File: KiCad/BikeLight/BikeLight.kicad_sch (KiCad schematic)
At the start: 19 parts, among them J1 Conn-01x02_P2.5mm_S2B-XH-A-BK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, J3 Conn-01x02_P2.5mm_S2B-XH-A-BK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, SW1 CK_KMS2xxG, U1 HT-CT62, U2 MPU-6050, U3 MCP1826S-33, U4 MAX17048, U5 TP4056-42-ESOP8, U6 MT3608, U7 RFID-RC522

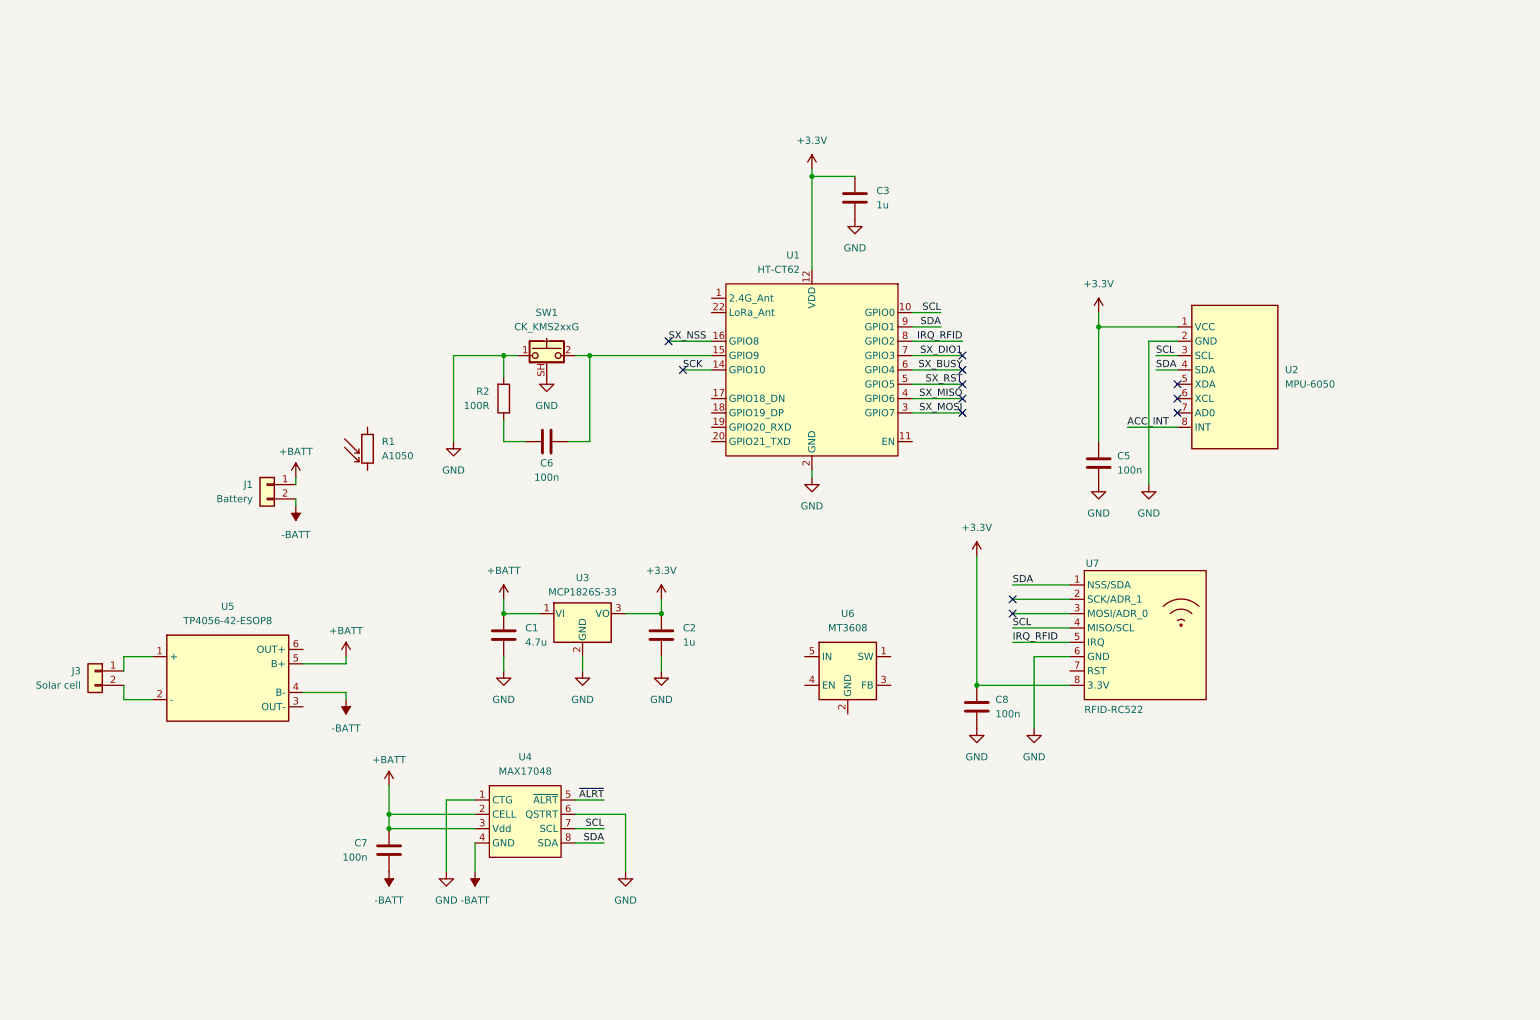
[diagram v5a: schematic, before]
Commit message: Added power protection, annotated
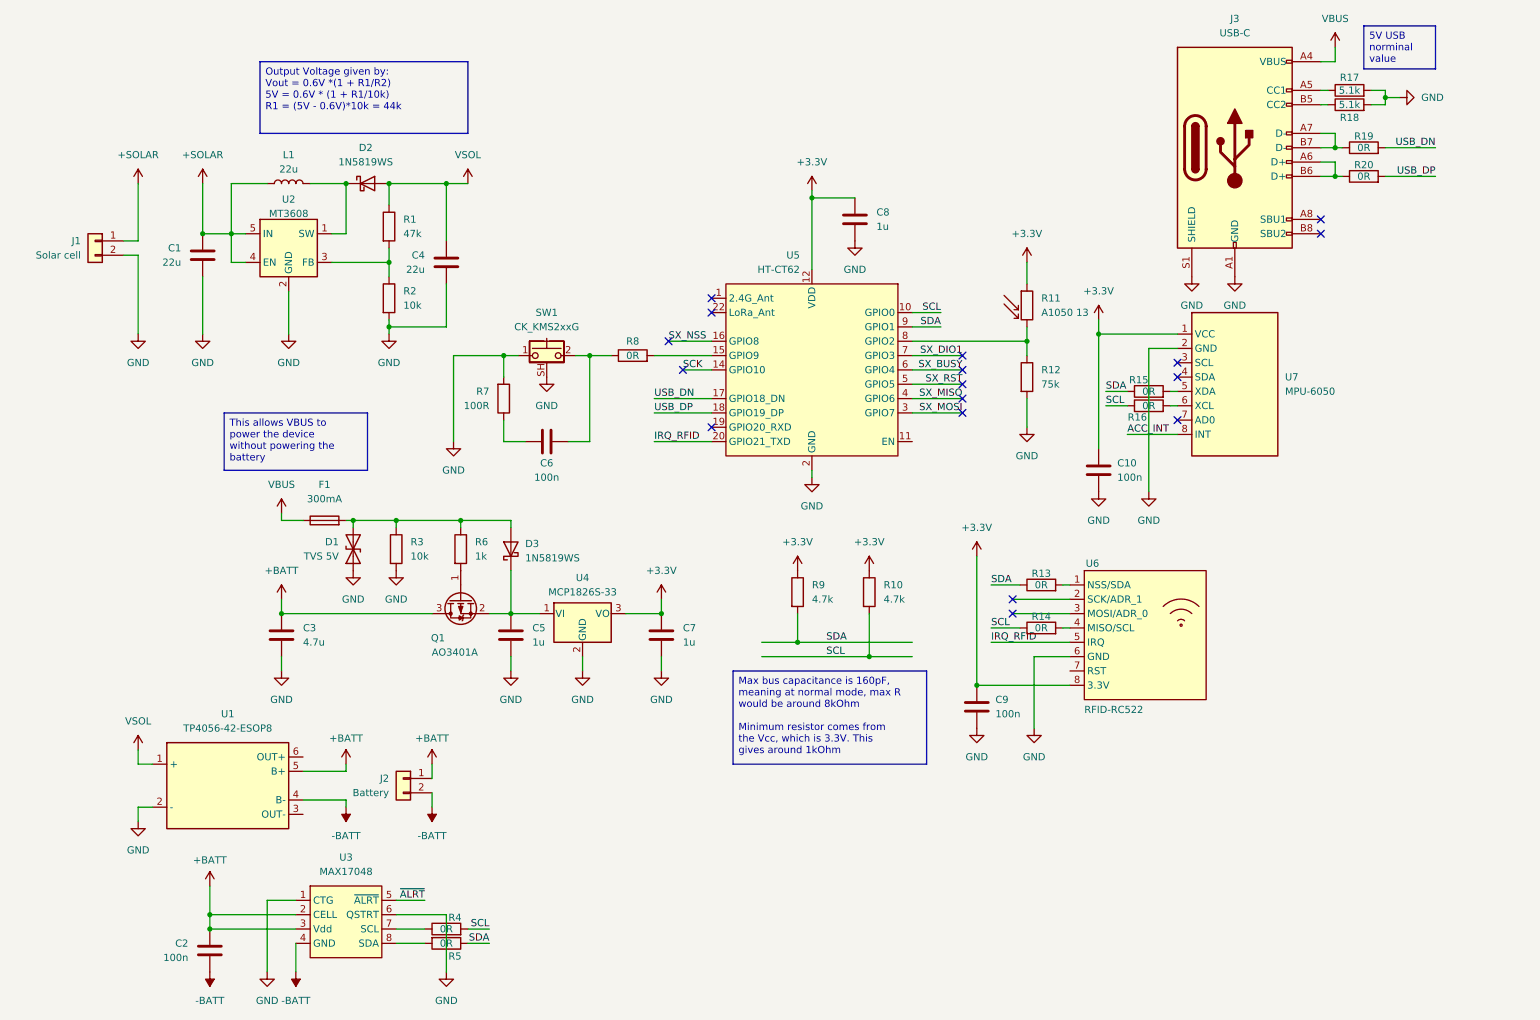
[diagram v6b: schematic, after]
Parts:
- added C1, C4: 22u_0805_CL21A226MAQNNNE, Capacitor_SMD:C_0805_2012Metric, symbol 00-kiml-capacitors-smd:22u_0805_CL21A226MAQNNNE
- added C5: 1u_0603_CL10A105KA8NNNC, Capacitor_SMD:C_0603_1608Metric, symbol 00-kiml-capacitors-smd:1u_0603_CL10A105KA8NNNC
- added D1: SOD-882_0402_RCLAMP0521P-N, Diode_SMD:D_0402_1005Metric, symbol 00-kiml-power-protection:SOD-882_0402_RCLAMP0521P-N
- added D2, D3: 1N5819WS, Diode_SMD:D_SOD-323, symbol 00-kiml-diode:1N5819WS
- added F1: MF-MSMF010-2, Fuse:Fuse_1812_4532Metric, symbol 00-kiml-power-protection:MF-MSMF010-2
- added J3: GT-USB-7051A, Connector_USB:USB_C_Receptacle_G-Switch_GT-USB-7051x, symbol 00-kiml-connector-usb:USB_C_Receptacle_USB2.0_TYPE-C-31-M-12
- added L1: 22u_620mA_1210_CBC3225T220KR, Inductor_SMD:L_1210_3225Metric, symbol 00-kiml-inductors:22u_620mA_1210_CBC3225T220KR
- added Q1: AO3401A, Package_TO_SOT_SMD:SOT-23, symbol 00-kiml-transistor-fet:AO3401A
- added R1: 47k_0402_0402WGF1002TCE, Resistor_SMD:R_0603_1608Metric, symbol 00-kiml-resistors-smd:47k_0402_0402WGF1002TCE
- added R10, R9: 4.7k_0402_0402WGF4701TCE, Resistor_SMD:R_0603_1608Metric, symbol 00-kiml-resistors-smd:4.7k_0402_0402WGF4701TCE
- added R12: 75k_0603_RC0603FR-0775KL, Resistor_SMD:R_0603_1608Metric, symbol 00-kiml-resistors-smd:75k_0603_RC0603FR-0775KL
- added R13, R14, R15, R16, R19, R20, R4, R5, R8: 0R_0603_0603WAF0000T5E, Resistor_SMD:R_0603_1608Metric, symbol 00-kiml-resistors-smd:0R_0603_0603WAF0000T5E
- added R17, R18: 5.1k_0603_0603WAF5101T5E, Resistor_SMD:R_0603_1608Metric, symbol 00-kiml-resistors-smd:5.1k_0603_0603WAF5101T5E
- added R2, R3: 10k_0603_RC0603JR-0710KL, Resistor_SMD:R_0603_1608Metric, symbol 00-kiml-resistors-smd:10k_0603_RC0603JR-0710KL
- added R6: 1k_0603_RMC06031K1%N, Resistor_SMD:R_0603_1608Metric, symbol 00-kiml-resistors-smd:1k_0603_RMC06031K1%N
- R11: renamed from R1; value A1050 -> A1050 13
- renumbered C5 to C10, C7 to C2, C1 to C3, C2 to C7, C3 to C8, C8 to C9, J3 to J1, J1 to J2, R2 to R7, U5 to U1, U6 to U2, U4 to U3, U3 to U4, U1 to U5, U7 to U6, U2 to U7
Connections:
- net +3.3V: now also R11.1, R10.1, R9.1
- net +BATT: now also Q1.3 (D); no longer U4.1 (VI)
- net GND: now also J1.2 (Pin_2), U1.2 (-), U2.2 (GND), C1.2, C4.2, C5.2, D1.1 (A1), J3.A1 (GND), J3.A12 (GND), J3.B1 (GND), J3.B12 (GND), J3.S1 (SHIELD), R12.2, R17.2, R18.2, R2.2, R3.2
- net IRQ_RFID: now also U5.20 (GPIO21_TXD); no longer U5.8 (GPIO2)
- net SCL: now also R10.2, R14.1, R16.1, R4.2; no longer U3.7 (SCL), U6.4 (MISO/SCL), U7.3 (SCL)
- net SDA: now also R13.1, R15.1, R5.1, R9.2; no longer U3.8 (SDA), U6.1 (NSS/SDA), U7.4 (SDA)
- net +SOLAR: now reaches J1.1 (Pin_1)
- net +SOLAR: now also U2.4 (EN), U2.5 (IN), C1.1, L1.1; no longer U1.1 (+)
- net at C6.2, SW1.2: now also R8.1; no longer U5.15 (GPIO9)
- net at U7.5 (XDA): now also R15.2
- net at U7.6 (XCL): now also R16.2
- net USB_DN: now reaches U5.17 (GPIO18_DN)
- net USB_DN: now also R19.2
- net USB_DP: now reaches U5.18 (GPIO19_DP)
- net USB_DP: now also R20.2
- net at U2.1 (SW): now also D2.1 (K), L1.2
- net at U2.3 (FB): now also R1.2, R2.1
- net at R11.2: now also U5.8 (GPIO2), R12.1
- new net: J3.A5 (CC1), R17.1
- new net: J3.A6 (D+), J3.B6 (D+), R20.1
- new net: J3.A7 (D-), J3.B7 (D-), R19.1
- new net: J3.B5 (CC2), R18.1
- new net: D1.2 (A2), D3.2 (A), F1.2, R3.1, R6.1
- new net: R13.2, U6.1 (NSS/SDA)
- new net: R14.2, U6.4 (MISO/SCL)
- new net: C5.1, D3.1 (K), Q1.2 (S), U4.1 (VI)
- new net: R4.1, U3.7 (SCL)
- new net: R5.2, U3.8 (SDA)
- new net: R8.2, U5.15 (GPIO9)
- new net: Q1.1 (G), R6.2
- new net VBUS: F1.1, J3.A4 (VBUS), J3.A9 (VBUS), J3.B4 (VBUS), J3.B9 (VBUS)
- new net VSOL: C4.1, D2.2 (A), R1.1, U1.1 (+)
- no-connect marks 12 -> 17
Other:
- title: (none) -> Bikelight
- moved on the sheet: C10, C2, C3, C8, J1, J2, R11, U1, U2, U3, U7

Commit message: Finished most of the PCB
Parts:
- added R21, R22: 0R_0603_0603WAF0000T5E, Resistor_SMD:R_0603_1608Metric, symbol 00-kiml-resistors-smd:0R_0603_0603WAF0000T5E
- U6: footprint (none) -> Personal_Library:RFID_RC522
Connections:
- net ACC_INT: now also U5.19 (GPIO20_RXD)
- net SCL: now also R22.1
- net SDA: now also R5.2, R21.1; no longer R5.1
- net VSOL: now also D2.1 (K); no longer D2.2 (A)
- net at L1.2, U2.1 (SW): now also D2.2 (A); no longer D2.1 (K)
- net at U7.3 (SCL): now also R22.2
- net at U7.4 (SDA): now also R21.2
- net at U3.8 (SDA): now also R5.1; no longer R5.2
- no-connect marks 17 -> 14
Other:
- moved on the sheet: D2, R5

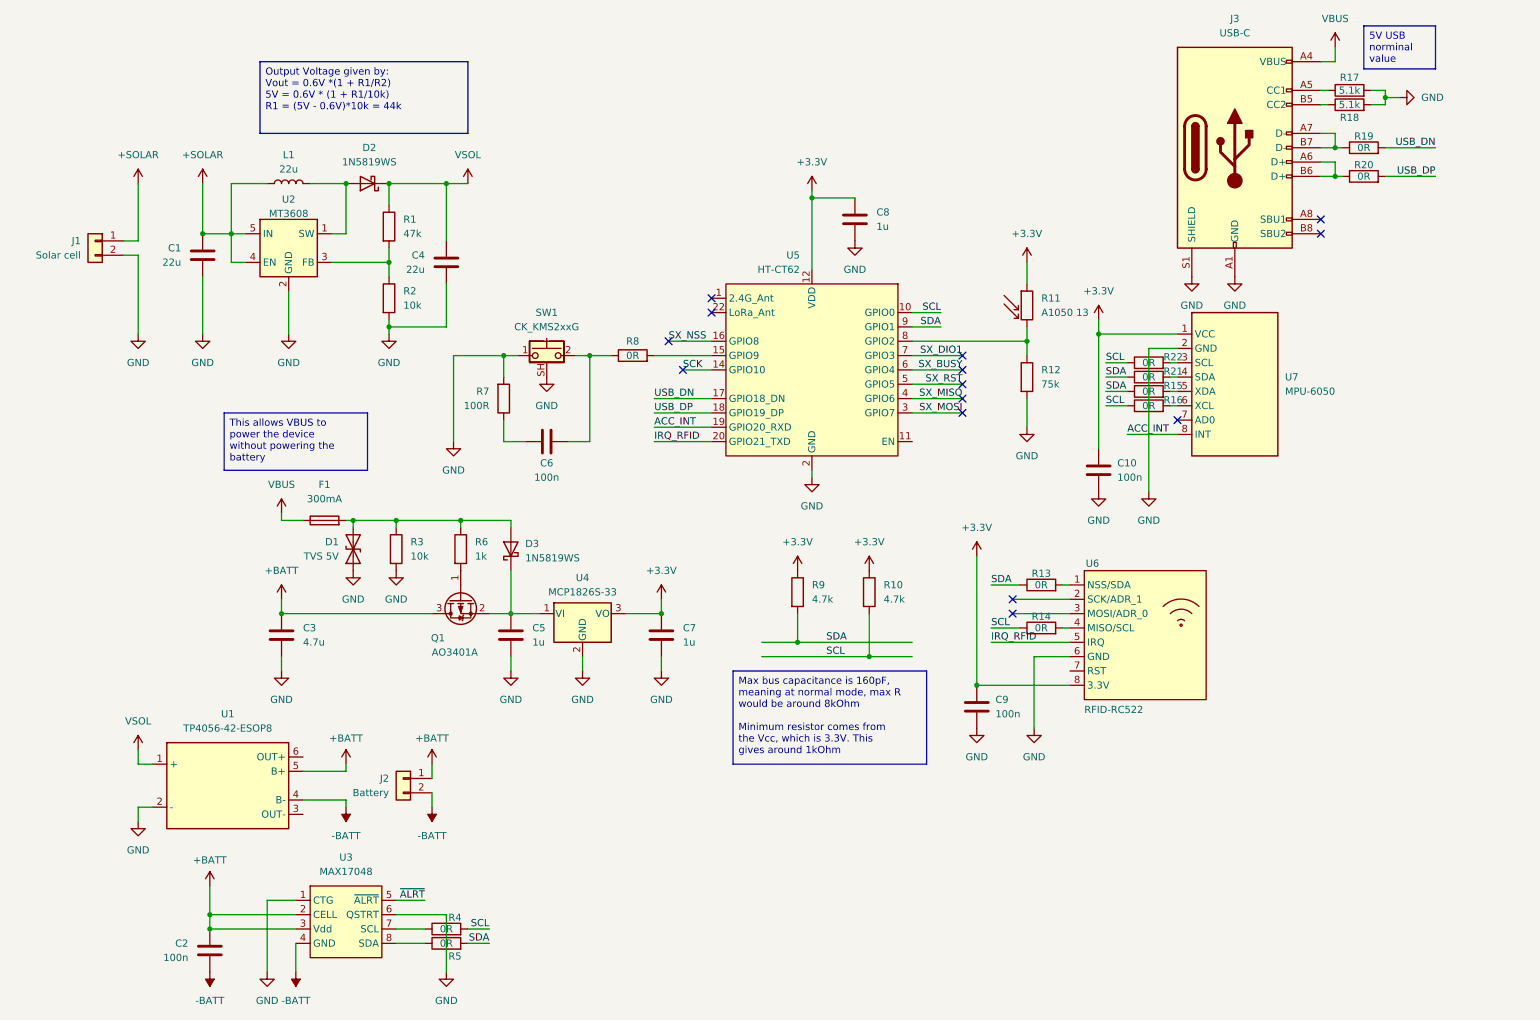
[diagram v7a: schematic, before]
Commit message: Added Busser and LED controller
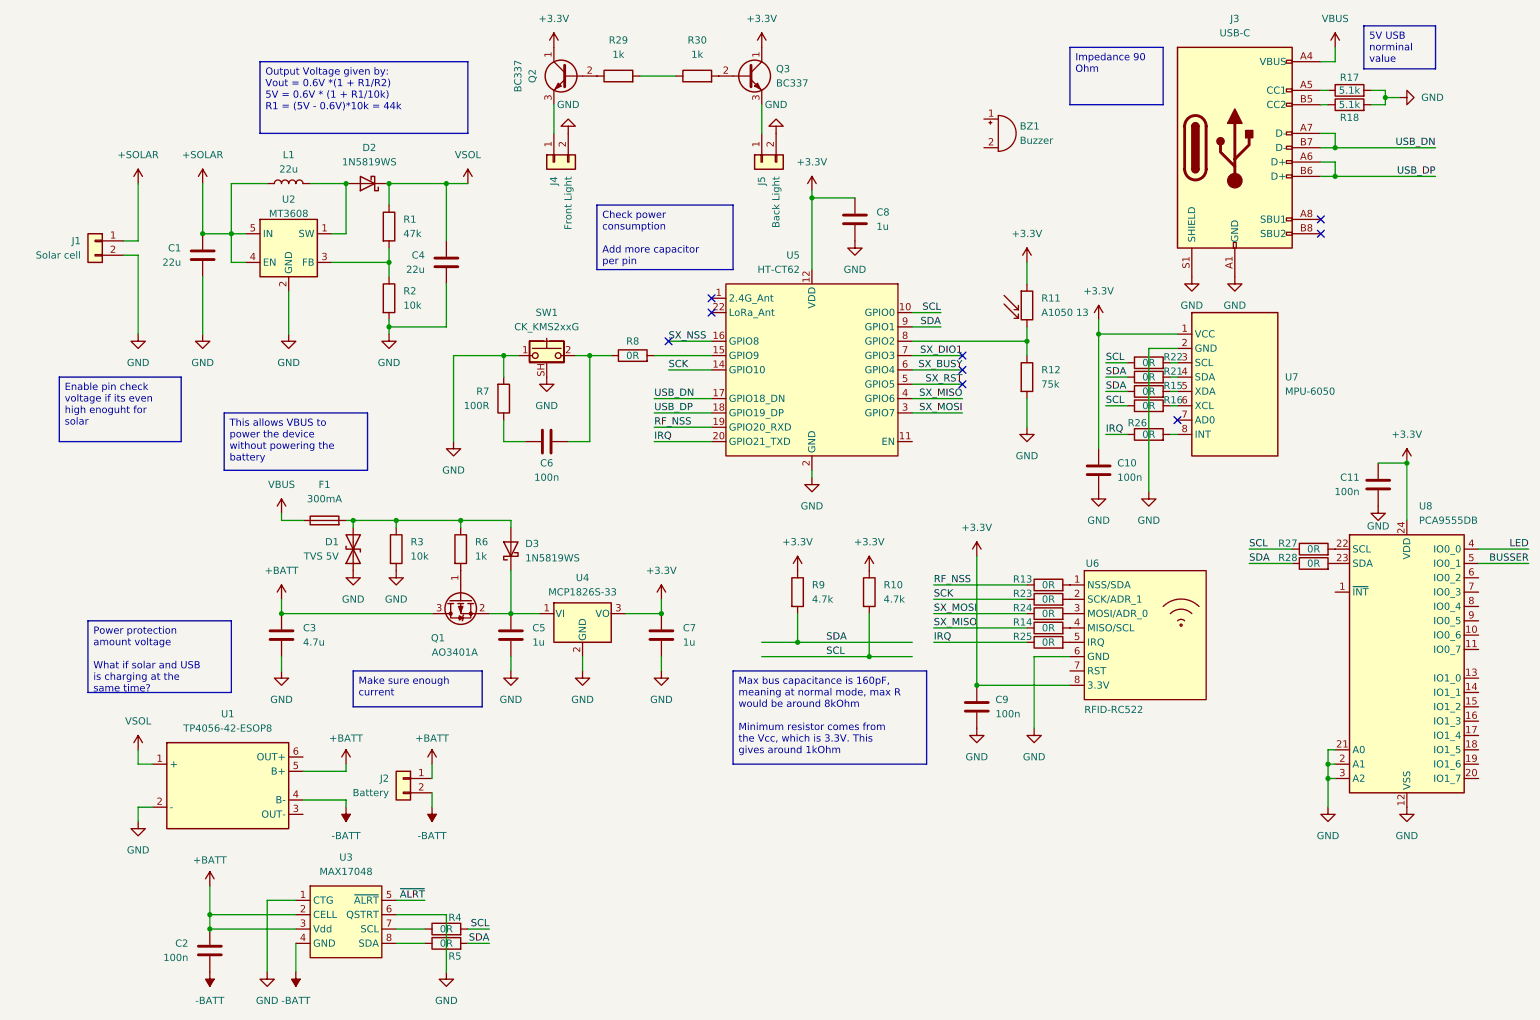
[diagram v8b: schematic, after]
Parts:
- removed R19, R20: 0R_0603_0603WAF0000T5E, Resistor_SMD:R_0603_1608Metric, symbol 00-kiml-resistors-smd:0R_0603_0603WAF0000T5E
- added BZ1: TMB12A03, Buzzer_Beeper:Buzzer_12x9.5RM7.6, symbol 00-kiml-buzzers:TMB12A03
- added C11: 100n_0603_TCC0603X7R104K500CT, Capacitor_SMD:C_0603_1608Metric, symbol 00-kiml-capacitors-smd:100n_0603_TCC0603X7R104K500CT
- added J4, J5: Conn-01x02_P2.5mm_S2B-XH-A-BK(LF)(SN), Connector_JST:JST_XH_S2B-XH-A_1x02_P2.50mm_Horizontal, symbol 00-kiml-connector-jst:Conn-01x02_P2.5mm_S2B-XH-A-BK(LF)(SN)
- added Q2, Q3: BC337, Package_TO_SOT_THT:TO-92_Inline, symbol Transistor_BJT:BC337
- added R23, R24, R25, R26, R27, R28: 0R_0603_0603WAF0000T5E, Resistor_SMD:R_0603_1608Metric, symbol 00-kiml-resistors-smd:0R_0603_0603WAF0000T5E
- added R29, R30: 1k_0603_RMC06031K1%N, Resistor_SMD:R_0603_1608Metric, symbol 00-kiml-resistors-smd:1k_0603_RMC06031K1%N
- added U8: PCA9555DB, Package_SO:SSOP-24_5.3x8.2mm_P0.65mm, symbol Interface_Expansion:PCA9555DB
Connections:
- net +3.3V: now also C11.1, Q2.1 (C), Q3.1 (C), U8.24 (VDD)
- net GND: now also C11.2, J4.2 (Pin_2), J5.2 (Pin_2), U8.12 (VSS), U8.2 (A1), U8.21 (A0), U8.3 (A2)
- net SCK: now also R23.1
- net SCL: now also R27.1; no longer R14.1
- net SDA: now also R28.1; no longer R13.1
- net SX_MISO: now also R14.1
- net SX_MOSI: now also R24.1
- net USB_DN: now also J3.A7 (D-), J3.B7 (D-)
- net USB_DP: now also J3.A6 (D+), J3.B6 (D+)
- net at U6.2 (SCK/ADR_1): now also R23.2
- net at U6.3 (MOSI/ADR_0): now also R24.2
- net ACC_INT: no longer names the net of U7.8 (INT)
- net ACC_INT: now also R26.2; no longer U5.19 (GPIO20_RXD)
- net IRQ_RFID: no longer names the net of U6.5 (IRQ)
- net IRQ_RFID: now also R25.2; no longer U5.20 (GPIO21_TXD)
- new net: R28.2, U8.23 (SDA)
- new net: R29.2, R30.1
- new net: Q3.2 (B), R30.2
- new net: J4.1 (Pin_1), Q2.3 (E)
- new net: J5.1 (Pin_1), Q3.3 (E)
- new net: Q2.2 (B), R29.1
- new net: R27.2, U8.22 (SCL)
- new net BUSSER: U8.5 (IO0_1)
- new net IRQ: R25.1, R26.1, U5.20 (GPIO21_TXD)
- new net LED: U8.4 (IO0_0)
- new net RF_NSS: R13.1, U5.19 (GPIO20_RXD)
- no-connect marks 14 -> 9
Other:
- moved on the sheet: R13, R14
